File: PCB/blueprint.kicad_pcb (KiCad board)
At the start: 2 copper layers, 41.5 x 67 mm, 7 parts, among them SW1 SW_Push, SW2 SW_Push, SW3 SW_Push, SW4 SW_Push, U1 XIAO-RP2040-DIP

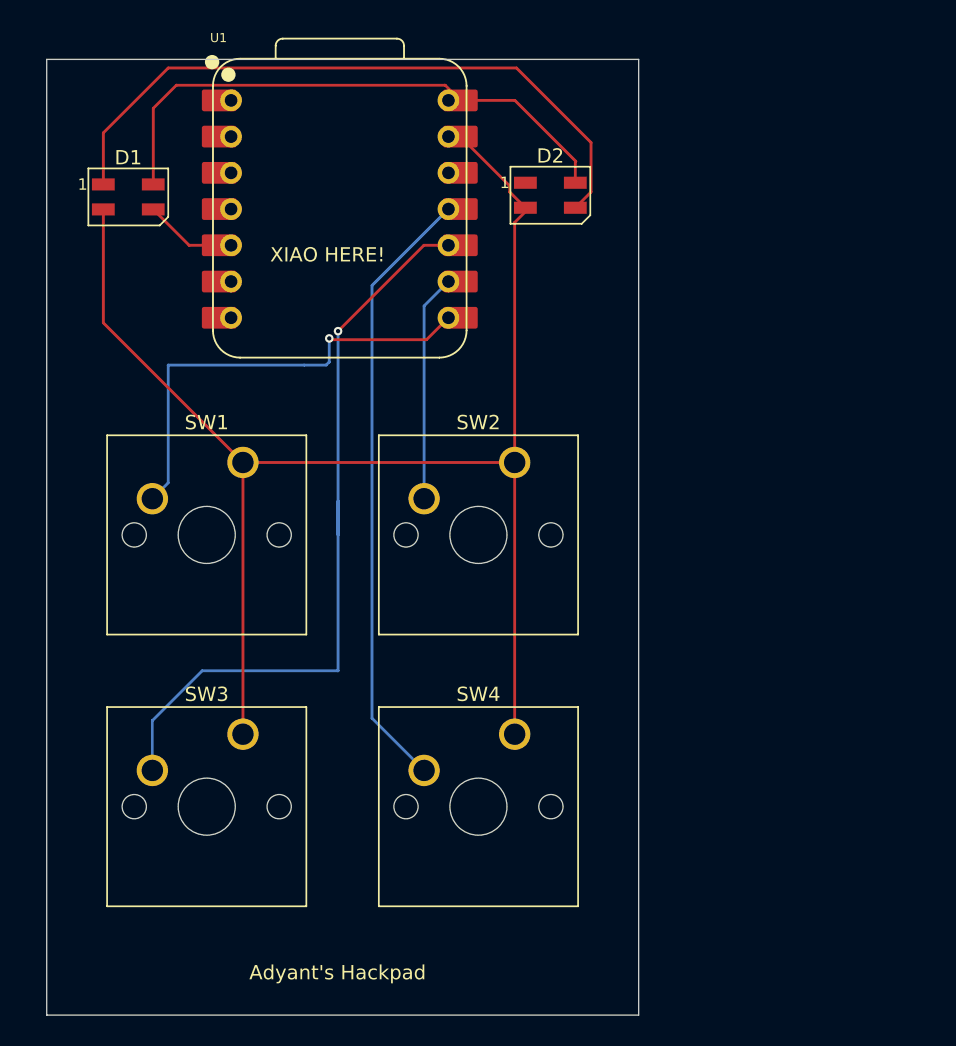
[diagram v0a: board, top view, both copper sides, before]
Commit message: Updated CAD and PCB for new Bear Case and layout
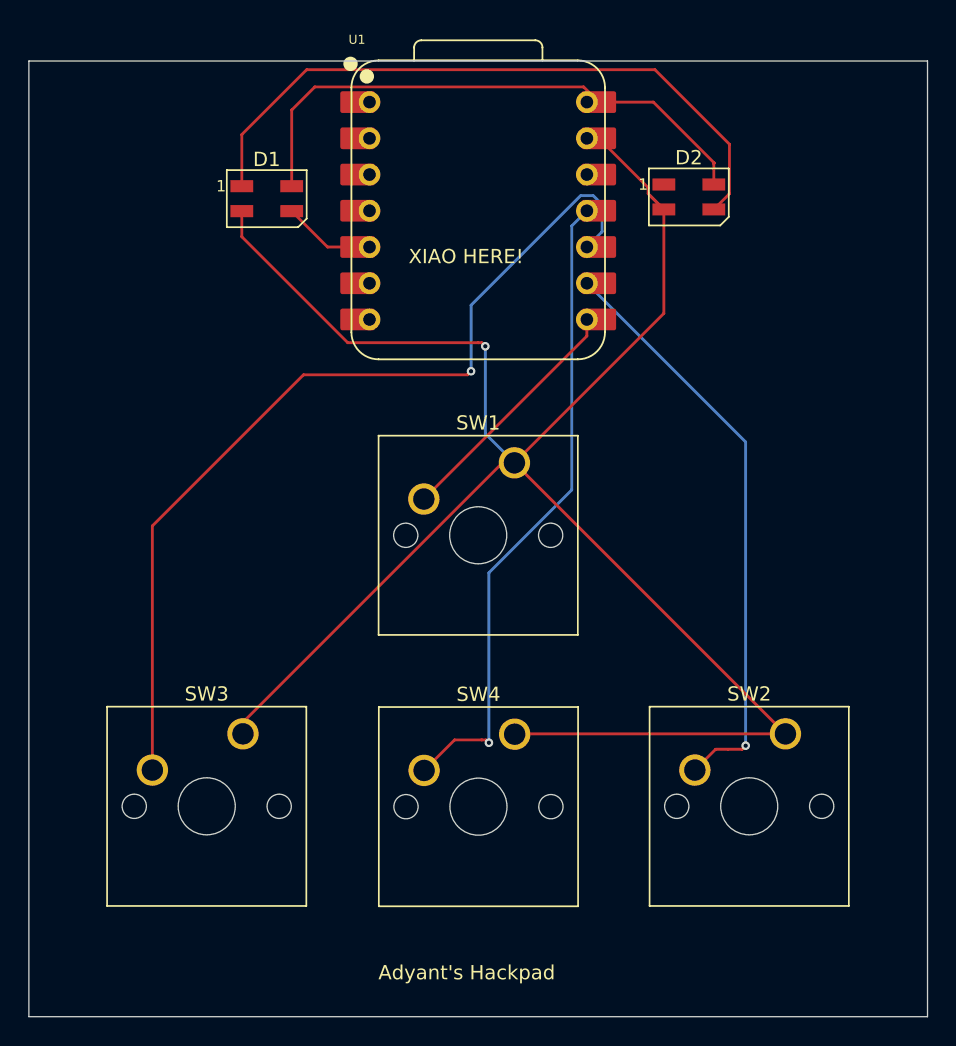
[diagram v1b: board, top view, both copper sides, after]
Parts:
- moved SW2 26.9 mm to (193.3, 99.7)
- moved SW1 19.0 mm to (174.3, 80.7)
- moved D1 9.71 mm to (156.9, 62.1)
- moved U1 9.71 mm to (171.8, 63.0)
- moved D2 9.71 mm to (186.5, 62.0)
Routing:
- net GND: track 104.0 -> 134.7 mm, vias 0 -> 1
- net Net-(U1-GPIO2/SCK): track 15.9 -> 41.3 mm, vias 0 -> 1
- net Net-(U1-GPIO1/RX): track 31.9 -> 17.3 mm, vias 1 -> 0
- net Net-(U1-GPIO4/MISO): track 56.8 -> 65.3 mm
- net Net-(U1-GPIO3/MOSI): track 43.1 -> 46.3 mm, vias 0 -> 1
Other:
- board size 41.5 x 67 mm -> 63 x 67 mm
